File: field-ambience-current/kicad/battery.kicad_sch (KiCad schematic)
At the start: 20 parts, among them J9 JST PH 2.0 2-pin (LiPo Batter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, U7 MCP73831T-2ACI/OT (LiPo Charg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, U8 TPS61089RNR (Boost LiPo→5V, 2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

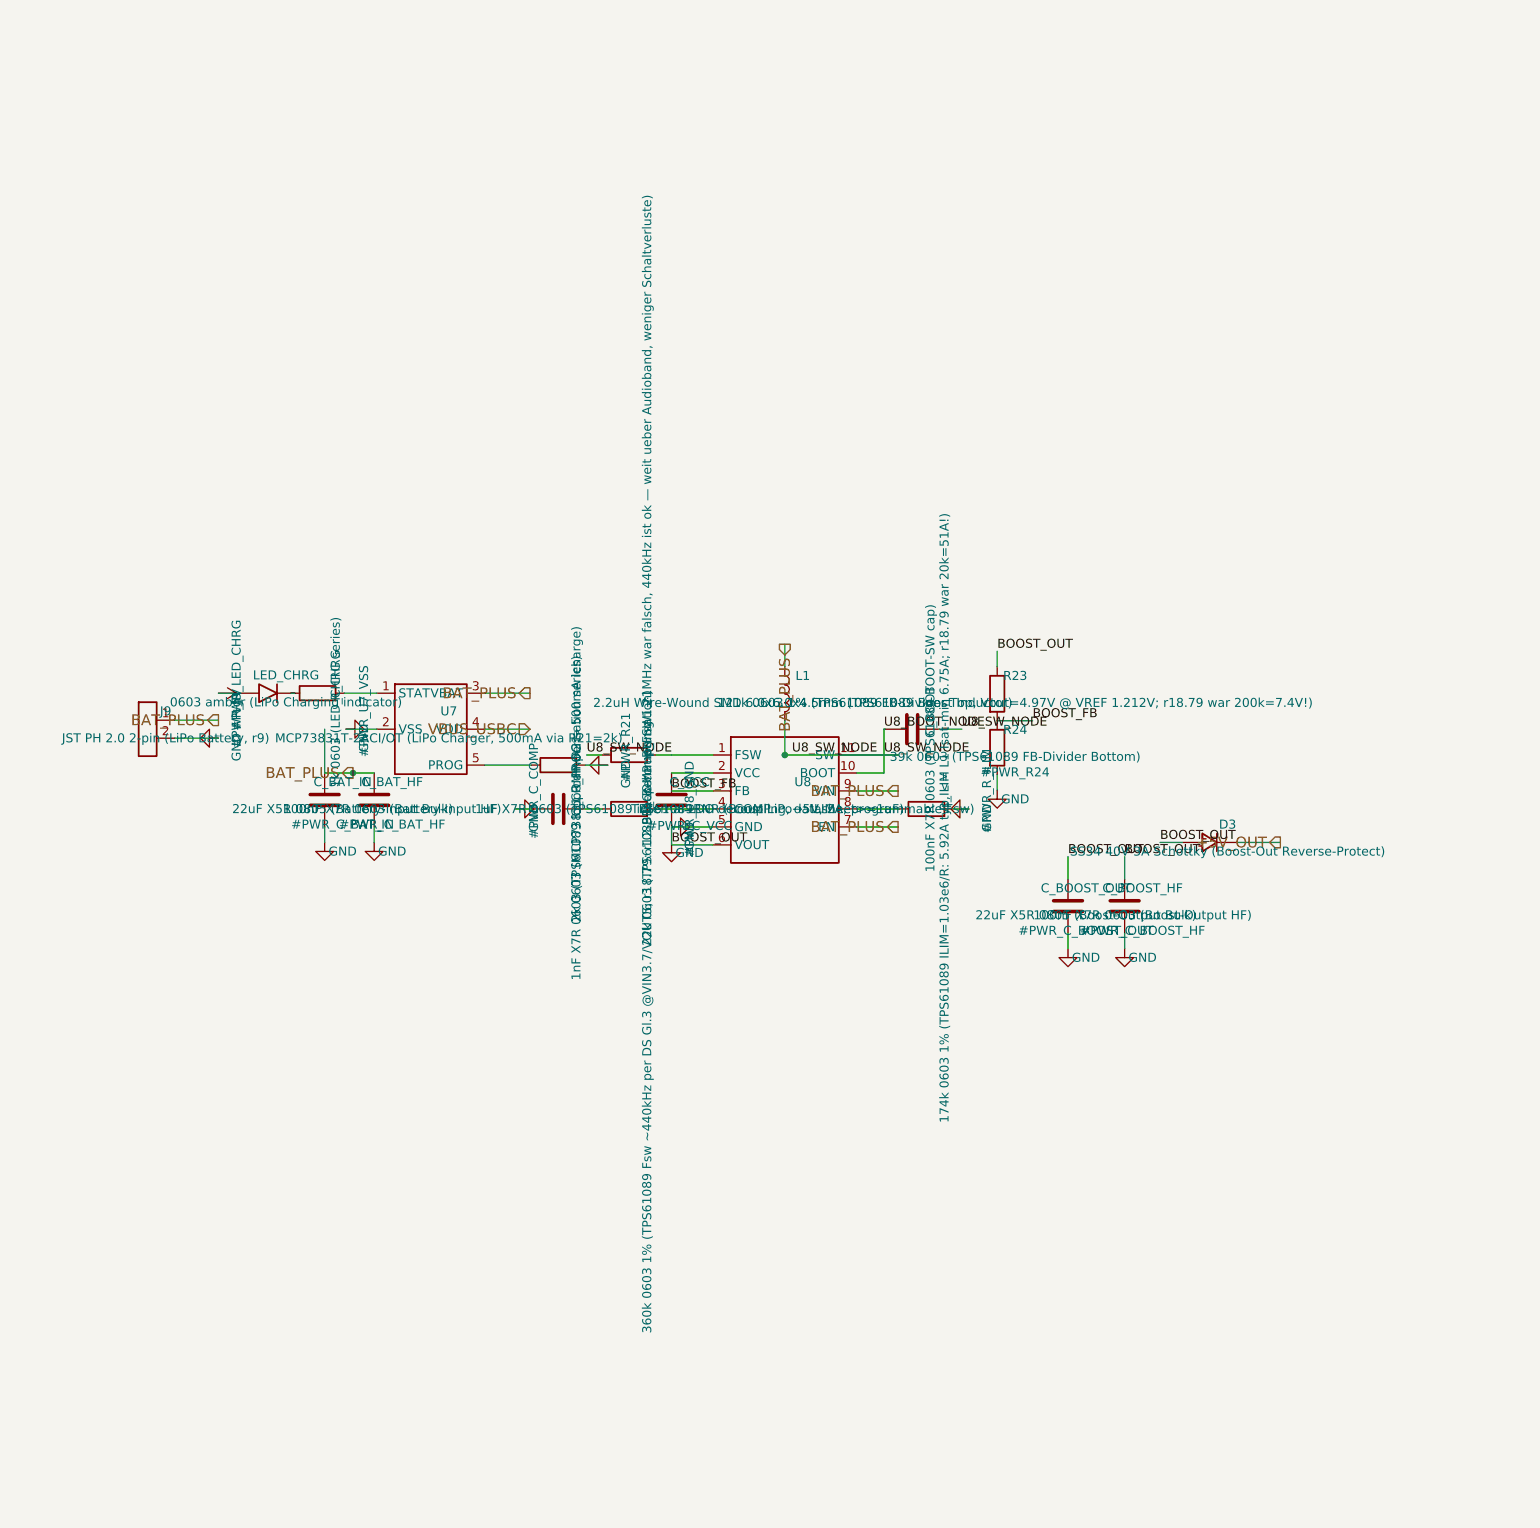
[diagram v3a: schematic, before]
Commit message: fix(pcb): geometric pin-level ERC — 7 copper shorts, 4 open circuits, boost loop instability (r18.80) (#92)
Headless geometric ERC (every pin anchor vs every wire segment, union-find
net build, hier-label/root-pin matching) over all 7 sheets found 12 real
defects; each verified in generator source and fixed there.

Copper shorts (pin/label anchors landing on foreign wires):
- power_tree: USB D+ AND D- hard-shorted to +5V — the U5 LDO block sat in
  the USB data corridor (EN pin on the DP wire, IN pin on the DM wire,
  rail drop overlapping the ESD VBUS wire). Block moved to (130,130).
- mcp: I2C_SCL shorted to GND — C5's GND pin landed exactly on the SCL
  wire (VDD pin 9 and SCL pin 12 are exactly 3 grid rows = 7.62mm apart,
  the cap's pin pitch). Entire I2C bus (U2+U6+U10) was dead. C5/C5b moved.
- audio: PCM_XSMT and I2S_LRCK shorted to GND (same 7.62mm trap, C8a/C8b
  and C_LDOO) — DAC permanently muted / no word clock. Caps flipped up.
- stm32: BOOT0 permanently HIGH twice over (+3V3 flag placed on the BOOT0
  node point; SW_BOOT wire drawn through its own pin-2 anchor) — MCU would
  always enter the ROM bootloader, never firmware.
- stm32: VDDA copper-tied to VDD (pin-21 stub drawn through the VDD pin-100
  anchor), bypassing FB2.
- battery: U8_SW_NODE label sat on the SW/BOOT wire crossing, merging the
  bootstrap net with the switch node (C_BOOT ineffective).

Open circuits:
- lcd: J3 LCD header — all 8 pins floating (wiring assumed KiCad-standard
  pins at -5.08 left; custom lib has pins at +3.81 right). J3 rotated 180.
- stm32: J4 SWD header — all 3 pins floating (same assumption). Board was
  unprogrammable.
- stm32: FB2 rotated 90 off its wires — both pins floating (VDDA had no
  intended supply path).
- stm32: lib_symbols entry lacked the MCU: prefix — KiCad cannot resolve
  U1 at all (exact lib_id match required).

Boost control loop (TPS61089, TI SLVSD38C eqs 15/17/18, validated by
reproducing TI's own 9V/2A reference values):
- R_COMP 22k -> 6.2k (n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
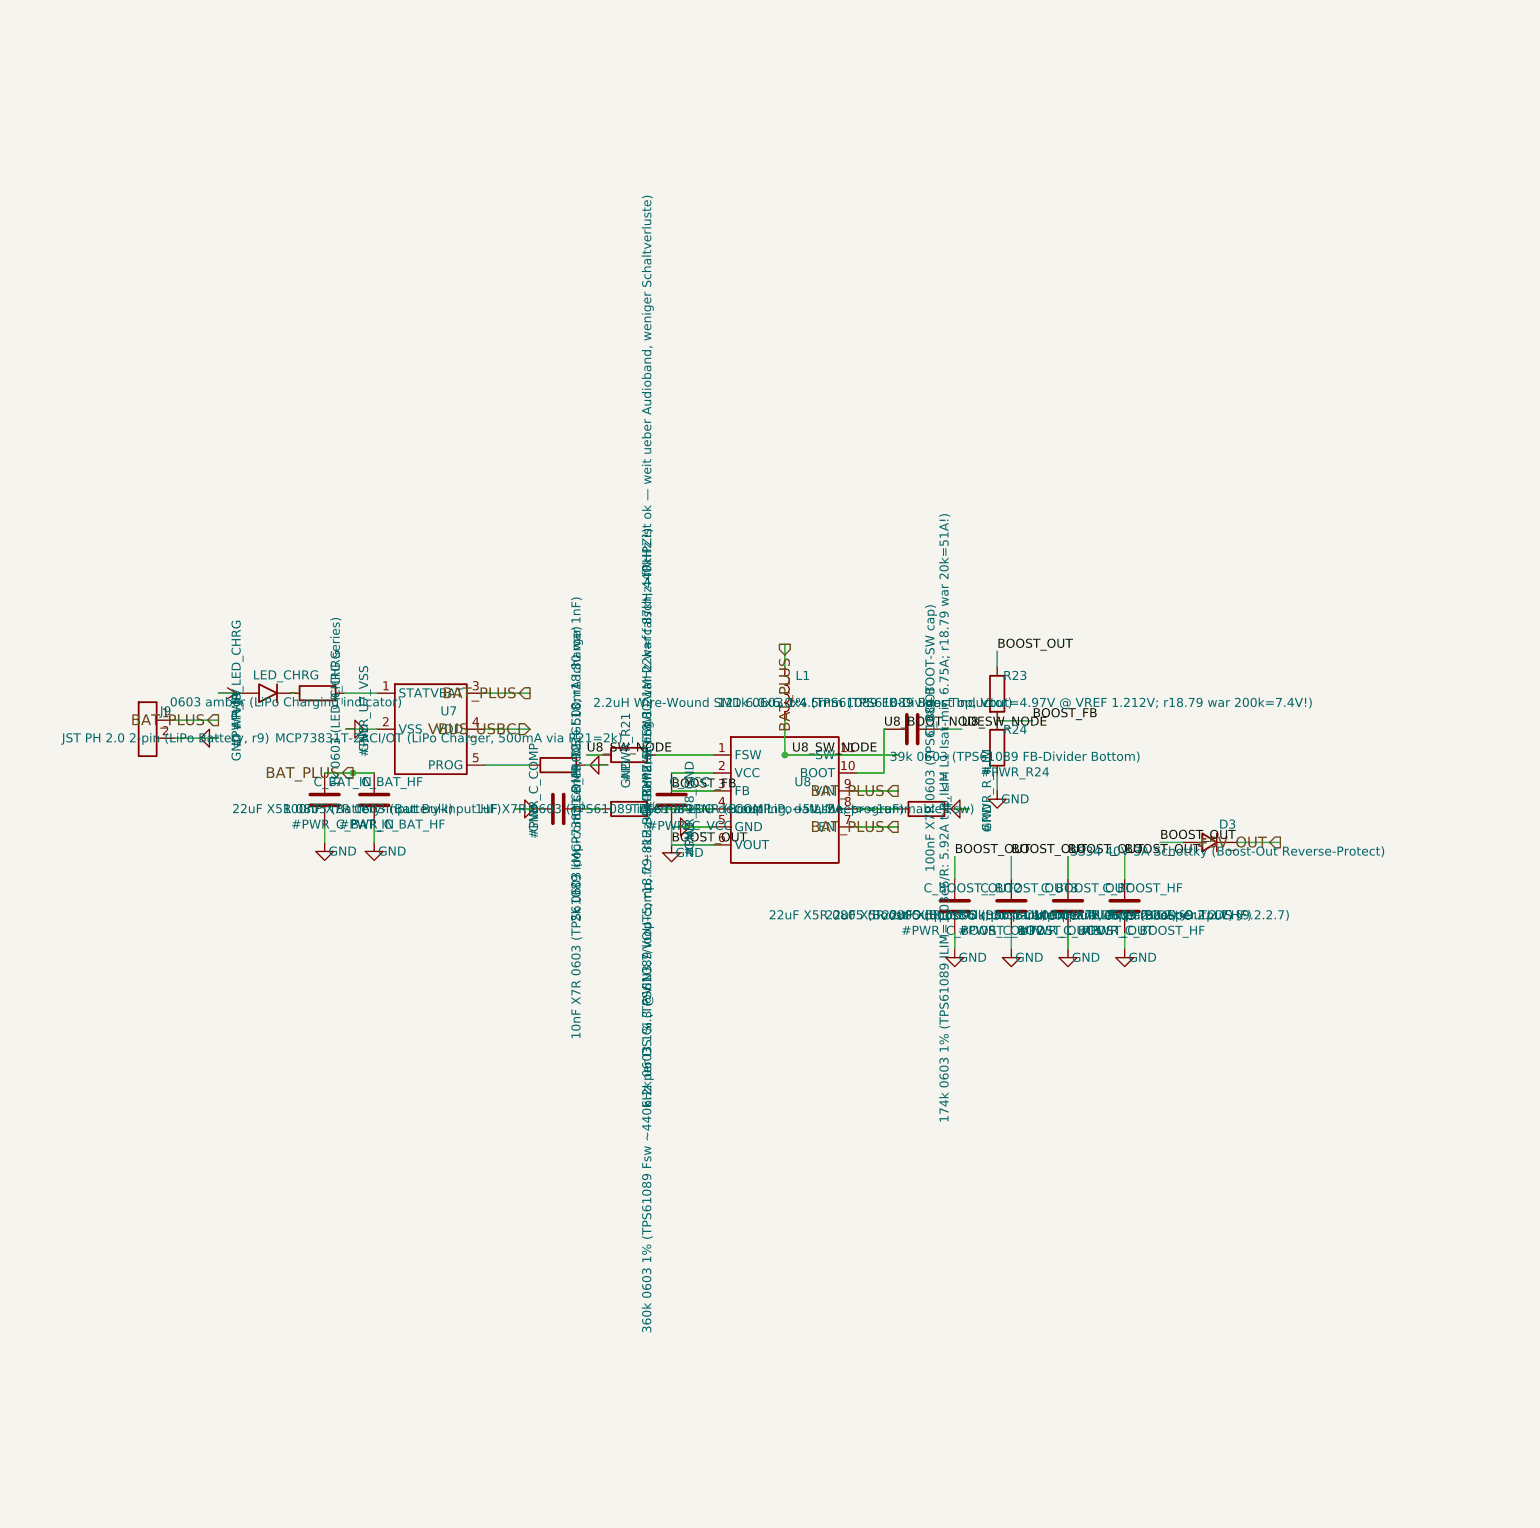
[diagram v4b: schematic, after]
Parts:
- added C_BOOST_OUT2, C_BOOST_OUT3: 22uF X5R 0805 (Boost-Output Bulk, 3x parallel per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, Capacitor_SMD:C_0805_2012Metric, symbol Device:C
- C_BAT_HF, C_BOOST_HF, C_BOOT: MPN CL10B104KO8NNNC -> CC0603KRX7R9BB104
- C_BAT_IN: MPN GRM21BR61E226ME44 -> CL21A226MAQNNNE
- C_BOOST_OUT: value 22uF X5R 0805 (Boost-Output Bulk) -> 22uF X5R 0805 (Boost-Output Bulk, 3x parallel per TI DS §9.2.2.7); MPN GRM21BR61E226ME44 -> CL21A226MAQNNNE
- C_COMP: value 1nF X7R 0603 (TPS61089 loop-compensation series) -> 10nF X7R 0603 (TPS61089 loop-comp series, DS Gl.18; r18.80 war 1nF); LCSC C1588 -> C57112; MPN CL10B102KB8NNNC -> 0603B103K500NT
- R_COMP: value 22k 0603 (TPS61089 loop-compensation) -> 6.2k 0603 1% (TPS61089 loop-comp, fc~8kHz<=fRHPZ/5; r18.80 war 22k=fc 87kHz>fRHPZ!); LCSC C31850 -> C4260; MPN 0603WAF2202T5E -> 0603WAF6201T5E
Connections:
- net BOOST_OUT: now also C_BOOST_OUT2.1, C_BOOST_OUT3.1
- net GND: now also C_BOOST_OUT2.2, C_BOOST_OUT3.2
- net U8_BOOT_NODE: no longer C_BOOT.2, L1.2, R_FSW.1, U8.11 (SW)
- new net U8_SW_NODE: C_BOOT.2, L1.2, R_FSW.1, U8.11 (SW)
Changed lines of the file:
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@@
       (property "Datasheet" "~" (at 75 90 0)
         (effects (font (size 1.27 1.27)) hide))
-      (property "MPN" "GRM21BR61E226ME44" (at 77.54 93.81 0)
+      (property "MPN" "CL21A226MAQNNNE" (at 77.54 93.81 0)
         (effects (font (size 1.27 1.27)) hide))
       (property "LCSC" "C45783" (at 77.54 95.08 0)
@@
       (property "Datasheet" "~" (at 82 90 0)
         (effects (font (size 1.27 1.27)) hide))
-      (property "MPN" "CL10B104KO8NNNC" (at 84.54 93.81 0)
+      (property "MPN" "CC0603KRX7R9BB104" (at 84.54 93.81 0)
         (effects (font (size 1.27 1.27)) hide))
       (property "LCSC" "C14663" (at 84.54 95.08 0)
@@
       (property "Datasheet" "~" (at 158 80 0)
         (effects (font (size 1.27 1.27)) hide))
-      (property "MPN" "CL10B104KO8NNNC" (at 160.54 83.81 0)
+      (property "MPN" "CC0603KRX7R9BB104" (at 160.54 83.81 0)
         (effects (font (size 1.27 1.27)) hide))
       (property "LCSC" "C14663" (at 160.54 85.08 0)
@@
       (property "Reference" "R_COMP" (at 120.54 88.73 0)
         (effects (font (size 1.27 1.27))))
-      (property "Value" "22k 0603 (TPS61089 loop-compensation)" (at 120.54 92.54 0)
+      (property "Value" "6.2k 0603 1% (TPS61089 loop-comp, fc~8kHz<=fRHPZ/5; r18.80 war 22k=fc 87kHz>fRHPZ!)" (at 120.54 92.54 0)
         (effects (font (size 1.27 1.27))))
       (property "Footprint" "Resistor_SMD:R_0603_1608Metric" (at 118 91.27000000000001 0)
@@
       (property "Datasheet" "~" (at 118 91.27000000000001 0)
         (effects (font (size 1.27 1.27)) hide))
-      (property "MPN" "0603WAF2202T5E" (at 120.54 95.08000000000001 0)
-        (effects (font (size 1.27 1.27)) hide))
-      (property "LCSC" "C31850" (at 120.54 96.35000000000001 0)
+      (property "MPN" "0603WAF6201T5E" (at 120.54 95.08000000000001 0)
+        (effects (font (size 1.27 1.27)) hide))
+      (property "LCSC" "C4260" (at 120.54 96.35000000000001 0)
         (effects (font (size 1.27 1.27)) hide))
     (instances
@@
       (property "Reference" "C_COMP" (at 110.54 88.73 0)
         (effects (font (size 1.27 1.27))))
-      (property "Value" "1nF X7R 0603 (TPS61089 loop-compensation series)" (at 110.54 92.54 0)
+      (property "Value" "10nF X7R 0603 (TPS61089 loop-comp series, DS Gl.18; r18.80 war 1nF)" (at 110.54 92.54 0)
         (effects (font (size 1.27 1.27))))
       (property "Footprint" "Capacitor_SMD:C_0603_1608Metric" (at 108 91.27000000000001 0)
@@
       (property "Datasheet" "~" (at 108 91.27000000000001 0)
         (effects (font (size 1.27 1.27)) hide))
-      (property "MPN" "CL10B102KB8NNNC" (at 110.54 95.08000000000001 0)
-        (effects (font (size 1.27 1.27)) hide))
-      (property "LCSC" "C1588" (at 110.54 96.35000000000001 0)
+      (property "MPN" "0603B103K500NT" (at 110.54 95.08000000000001 0)
+        (effects (font (size 1.27 1.27)) hide))
+      (property "LCSC" "C57112" (at 110.54 96.35000000000001 0)
         (effects (font (size 1.27 1.27)) hide))
     (instances
@@
       (property "Reference" "C_BOOST_OUT" (at 182.54 102.46 0)
         (effects (font (size 1.27 1.27))))
-      (property "Value" "22uF X5R 0805 (Boost-Output Bulk)" (at 182.54 106.27 0)
+      (property "Value" "22uF X5R 0805 (Boost-Output Bulk, 3x parallel per TI DS §9.2.2.7)" (at 182.54 106.27 0)
         (effects (font (size 1.27 1.27))))
       (property "Footprint" "Capacitor_SMD:C_0805_2012Metric" (at 180 105 0)
@@
       (property "Datasheet" "~" (at 180 105 0)
         (effects (font (size 1.27 1.27)) hide))
-      (property "MPN" "GRM21BR61E226ME44" (at 182.54 108.81 0)
+      (property "MPN" "CL21A226MAQNNNE" (at 182.54 108.81 0)
         (effects (font (size 1.27 1.27)) hide))
       (property "LCSC" "C45783" (at 182.54 110.08 0)
@@
       (project "field_ambience"
         (path "/f6a664dc-7032-4108-a10b-e4076008e6bd" (reference "#PWR_C_BOOST_OUT") (unit 1)))))
+  (symbol (lib_id "Device:C") (at 164 105 0) (unit 1)
+    (in_bom yes) (on_board yes) (dnp no)
+      (property "Reference" "C_BOOST_OUT2" (at 166.54 102.46 0)
+        (effects (font (size 1.27 1.27))))
+      (property "Value" "22uF X5R 0805 (Boost-Output Bulk, 3x parallel per TI DS §9.2.2.7)" (at 166.54 106.27 0)
+        (effects (font (size 1.27 1.27))))
+      (property "Footprint" "Capacitor_SMD:C_0805_2012Metric" (at 164 105 0)
+        (effects (font (size 1.27 1.27)) hide))
+      (property "Datasheet" "~" (at 164 105 0)
+        (effects (font (size 1.27 1.27)) hide))
+      (property "MPN" "CL21A226MAQNNNE" (at 166.54 108.81 0)
+        (effects (font (size 1.27 1.27)) hide))
+      (property "LCSC" "C45783" (at 166.54 110.08 0)
+        (effects (font (size 1.27 1.27)) hide))
+    (instances
+      (project "field_ambience"
+        (path "/f6a664dc-7032-4108-a10b-e4076008e6bd" (reference "C_BOOST_OUT2") (unit 1)))))
+  (symbol (lib_id "Power:GND") (at 164 111 0) (unit 1)
+    (in_bom yes) (on_board yes) (dnp no)
+      (property "Reference" "#PWR_C_BOOST_OUT2" (at 166.54 108.46 0)
+        (effects (font (size 1.27 1.27))))
+      (property "Value" "GND" (at 166.54 112.27 0)
+        (effects (font (size 1.27 1.27))))
+      (property "Footprint" "" (at 164 111 0)
+        (effects (font (size 1.27 1.27)) hide))
+      (property "Datasheet" "~" (at 164 111 0)
+        (effects (font (size 1.27 1.27)) hide))
+    (instances
+      (project "field_ambience"
+        (path "/f6a664dc-7032-4108-a10b-e4076008e6bd" (reference "#PWR_C_BOOST_OUT2") (unit 1)))))
+  (symbol (lib_id "Device:C") (at 172 105 0) (unit 1)
+    (in_bom yes) (on_board yes) (dnp no)
+      (property "Reference" "C_BOOST_OUT3" (at 174.54 102.46 0)
+        (effects (font (size 1.27 1.27))))
+      (property "Value" "22uF X5R 0805 (Boost-Output Bulk, 3x parallel per TI DS §9.2.2.7)" (at 174.54 106.27 0)
+        (effects (font (size 1.27 1.27))))
+      (property "Footprint" "Capacitor_SMD:C_0805_2012Metric" (at 172 105 0)
+        (effects (font (size 1.27 1.27)) hide))
+      (property "Datasheet" "~" (at 172 105 0)
+        (effects (font (size 1.27 1.27)) hide))
+      (property "MPN" "CL21A226MAQNNNE" (at 174.54 108.81 0)
+        (effects (font (size 1.27 1.27)) hide))
+      (property "LCSC" "C45783" (at 174.54 110.08 0)
+        (effects (font (size 1.27 1.27)) hide))
+    (instances
+      (project "field_ambience"
+        (path "/f6a664dc-7032-4108-a10b-e4076008e6bd" (reference "C_BOOST_OUT3") (unit 1)))))
+  (symbol (lib_id "Power:GND") (at 172 111 0) (unit 1)
+    (in_bom yes) (on_board yes) (dnp no)
+      (property "Reference" "#PWR_C_BOOST_OUT3" (at 174.54 108.46 0)
+        (effects (font (size 1.27 1.27))))
+      (property "Value" "GND" (at 174.54 112.27 0)
+        (effects (font (size 1.27 1.27))))
+      (property "Footprint" "" (at 172 111 0)
+        (effects (font (size 1.27 1.27)) hide))
+      (property "Datasheet" "~" (at 172 111 0)
+        (effects (font (size 1.27 1.27)) hide))
+    (instances
+      (project "field_ambience"
+        (path "/f6a664dc-7032-4108-a10b-e4076008e6bd" (reference "#PWR_C_BOOST_OUT3") (unit 1)))))
   (symbol (lib_id "Device:C") (at 188 105 0) (unit 1)
     (in_bom yes) (on_board yes) (dnp no)
@@
       (property "Datasheet" "~" (at 188 105 0)
         (effects (font (size 1.27 1.27)) hide))
-      (property "MPN" "CL10B104KO8NNNC" (at 190.54 108.81 0)
+      (property "MPN" "CC0603KRX7R9BB104" (at 190.54 108.81 0)
         (effects (font (size 1.27 1.27)) hide))
       (property "LCSC" "C14663" (at 190.54 110.08 0)
@@
     (stroke (width 0) (type default))
 )
-  (wire (pts (xy 75 86.19) (xy 75 80))
-    (stroke (width 0) (type default))
-)
   (wire (pts (xy 75 86.19) (xy 79 86.19))
     (stroke (width 0) (type default))
@@
     (stroke (width 0) (type default))
 )
+  (wire (pts (xy 164 101.19) (xy 164 98))
+    (stroke (width 0) (type default))
+)
+  (wire (pts (xy 164 108.81) (xy 164 111))
+    (stroke (width 0) (type default))
+)
+  (wire (pts (xy 172 101.19) (xy 172 98))
+    (stroke (width 0) (type default))
+)
+  (wire (pts (xy 172 108.81) (xy 172 111))
+    (stroke (width 0) (type default))
+)
   (wire (pts (xy 188 101.19) (xy 188 98))
     (stroke (width 0) (type default))
@@
   (junction (at 140 83.65) (diameter 0) (color 0 0 0 0)
 )
-  (label "U8_SW_NODE" (at 154 83.65 0) (fields_autoplaced)
-    (effects (font (size 1.27 1.27)) (justify left bottom))
-)
   (label "U8_SW_NODE" (at 141 83.65 0) (fields_autoplaced)
     (effects (font (size 1.27 1.27)) (justify left bottom))
@@
     (effects (font (size 1.27 1.27)) (justify left bottom))
 )
+  (label "BOOST_OUT" (at 164 98 0) (fields_autoplaced)
+    (effects (font (size 1.27 1.27)) (justify left bottom))
+)
+  (label "BOOST_OUT" (at 172 98 0) (fields_autoplaced)
+    (effects (font (size 1.27 1.27)) (justify left bottom))
+)
